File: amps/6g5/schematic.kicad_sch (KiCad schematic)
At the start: 97 parts, among them SW1 AC

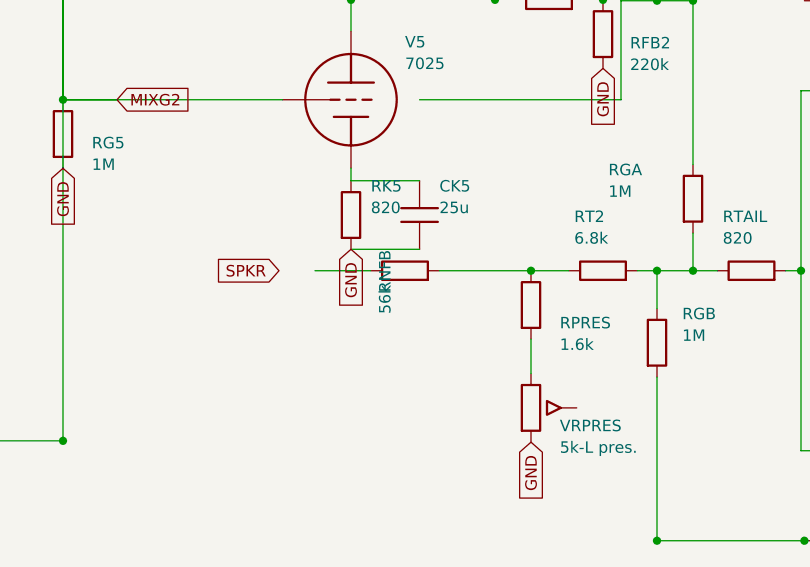
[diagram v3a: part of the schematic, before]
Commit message: Fix: 6G5 RNFB lettered vertically — label_rot pins the FILE angle
The re-shoot caught it at crop zoom: pinning label_rot=0 on a rot-90 body
renders the block vertically, because the renderer treats a property's angle
as symbol-relative — the compensation sym() applies by default (360 - rot)
was being overridden to nothing. The pin was redundant anyway: the authored
under-the-part anchor is the actual fix, and the default compensation
already letters it horizontally. Verified against the live render.

🤖 Generated with [Claude Code](https://claude.com/claude-code)

Co-Authored-By: Claude Fable 5 <noreply@anthropic.com>
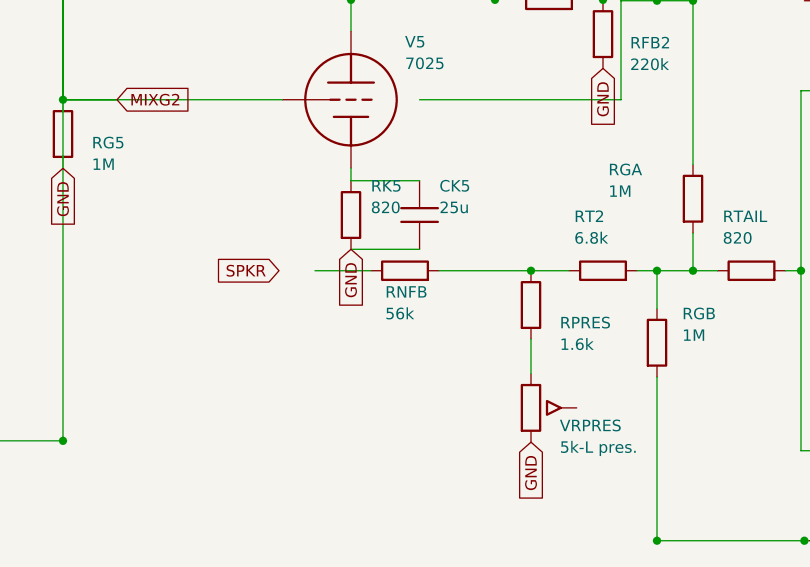
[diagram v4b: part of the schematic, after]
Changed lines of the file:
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@@
   (symbol (lib_id "cx:R") (at 216.745 109.82 90) (unit 1)
     (in_bom yes) (on_board yes)
-    (property "Reference" "RNFB" (at 214.545 112.22 0) (effects (font (size 1.27 1.27)) (justify left)))
-    (property "Value" "56k" (at 214.545 114.62 0) (effects (font (size 1.27 1.27)) (justify left))))
+    (property "Reference" "RNFB" (at 214.545 112.22 270) (effects (font (size 1.27 1.27)) (justify left)))
+    (property "Value" "56k" (at 214.545 114.62 270) (effects (font (size 1.27 1.27)) (justify left))))
   (wire (pts (xy 220.555 109.82) (xy 230.745 109.82))
     (stroke (width 0) (type default)))

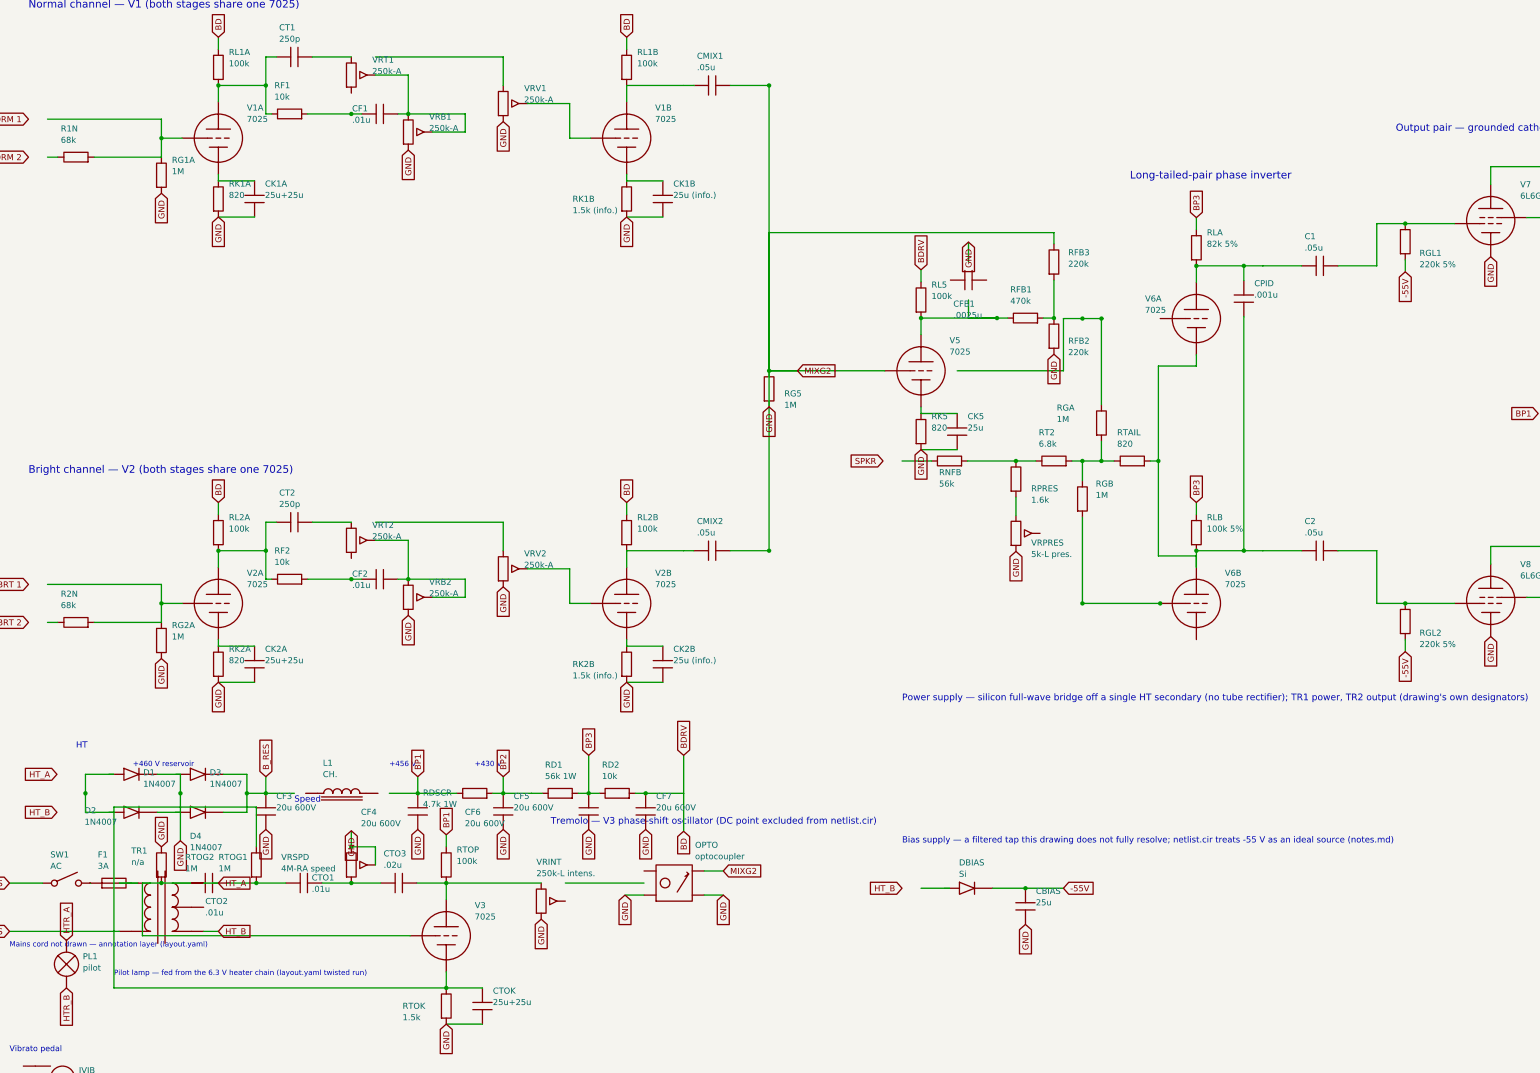
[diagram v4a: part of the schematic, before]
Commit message: Fix: deterministic schematic ids and wires split at every join
- _u() is uuid5 over (amp id, emission order), so a regeneration of an
  unchanged script is byte-identical and a drift gate becomes possible
- write() splits wire segments at symbol pins, wire ends and junction dots,
  so the file connects exactly what the drawing shows under KiCad's
  endpoint-only semantics (270 pins were on a wire's interior; net
  partitions unchanged on all 38 sheets)
- all sheets regenerated; aa864-bassman title block was stale (draft) and
  now matches meta.yaml (verified)

Co-Authored-By: Claude Fable 5.1 <noreply@anthropic.com>
Claude-Session: https://claude.ai/code/session_01KBMfdh37HmCL2iWcBiL5J1
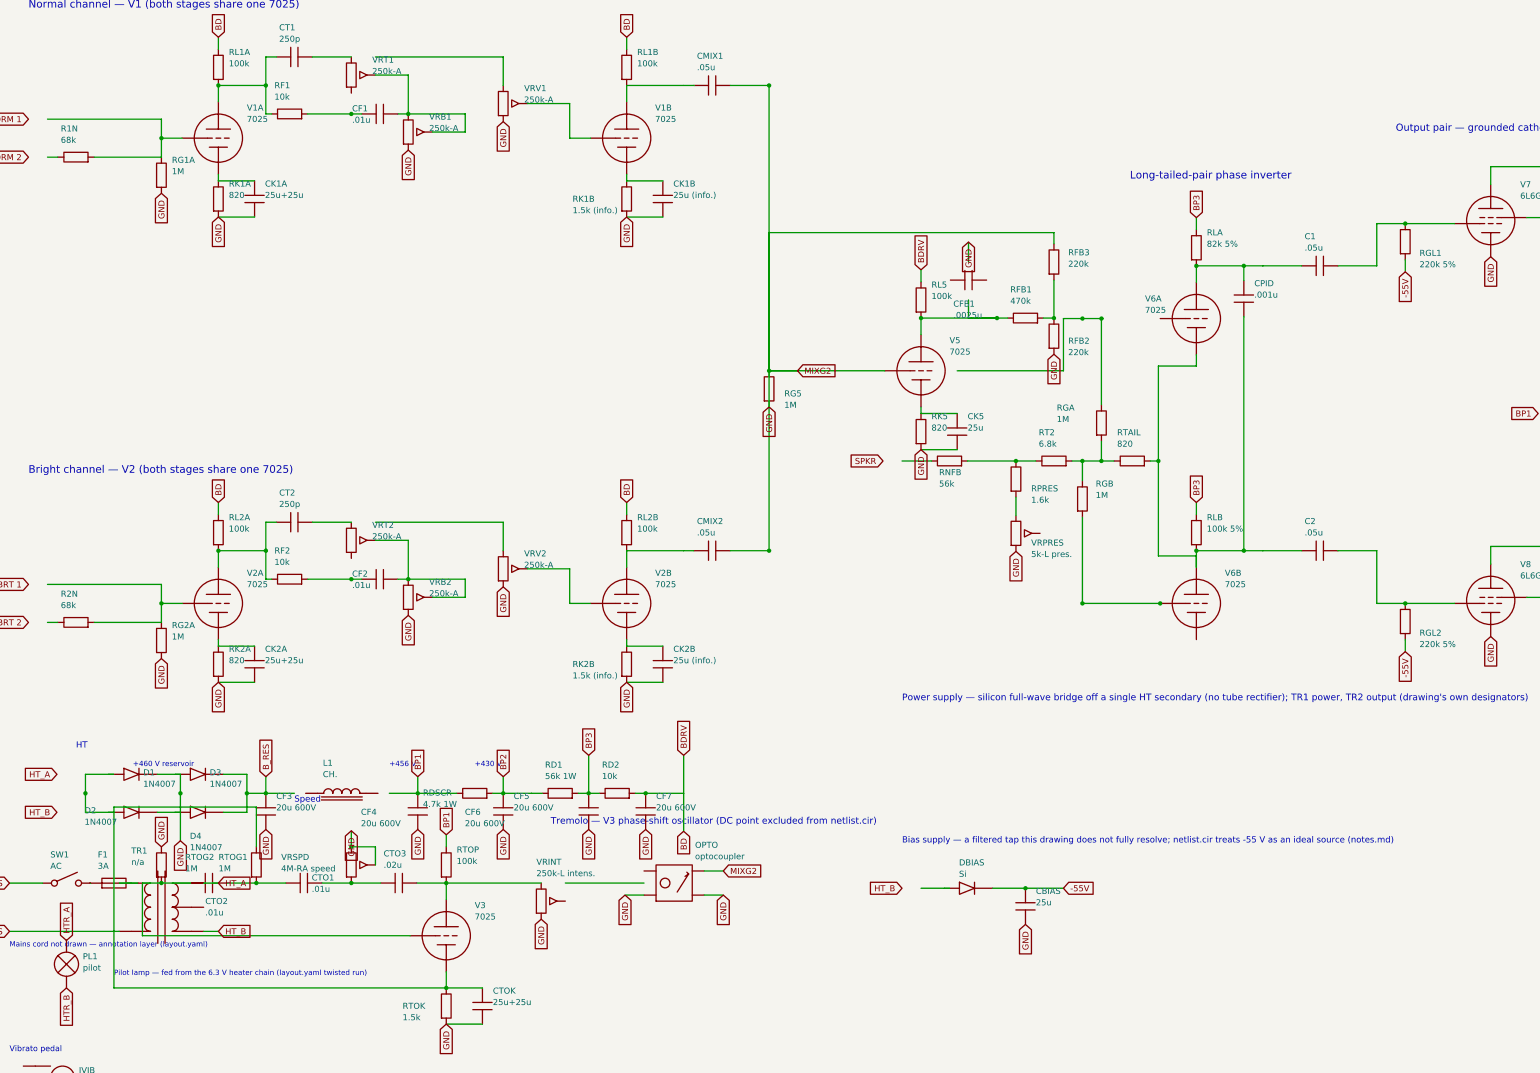
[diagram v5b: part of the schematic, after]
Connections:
- net GND: now also D3.1 (A), D4.1 (A)
- net at CTOK.1, RTOG1.1, RTOK.1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: now also D1.1 (A), D2.1 (A)

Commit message: Fix: schematic wiring on 6g3, 6g4, 6g5, 6g6b
- long-tailed pair tail moved off section B's plate to its cathode (6g3,
  6g4, 6g5); 6g4 V8 plate lead was drawn under its grounded cathode
- 6g6b: all five OT leads on bare coordinates with the secondary drawn on
  the primary side; bias line taken off the bleeder's grounded end (NBIAS
  and GND one net); both tone networks rebuilt; mixing bus ran through
  V3A's bottle
- eight parts shorted end to end, invisible to the pin check: 6g4 RGL1;
  6g5 RG5 (mixing node on ground); 6g6b C11, RG4B, RNFB, RTAIL, RTN1, VR3
- 6g5: treble pot runs off each other's lug, driver run 12 mm short of
  V6A grid, CFB1 rotated but wired upright, choke leads short both ends
- five dated waivers (bridge rectifier centre tap, footswitch terminal
  not lettered on the source, mains side outside the drawing, VR7's
  undesignated cap)
- OPEN, not guessed: 6g5 presence network is drawn as a DC path to ground
  (RPRES + pot in series) while netlist.cir has RT2 to ground and calls the
  network DC-neutral; sources do not settle it — sheet stays unclaimed

Co-Authored-By: Claude Fable 5.1 <noreply@anthropic.com>
Claude-Session: https://claude.ai/code/session_01KBMfdh37HmCL2iWcBiL5J1
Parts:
- removed CF7: 20u 600V, symbol cx:C
- removed JSPK: spkr, symbol cx:JACK
- removed L1: CH., symbol cx:CHOKE
- removed RLA: 82k 5%, symbol cx:R
- removed RNFB: 56k, symbol cx:R
- removed RSC1: 470 1W, symbol cx:R
- removed RT2: 6.8k, symbol cx:R
- removed RTOK: 1.5k, symbol cx:R
- added CTOK: 25u+25u, symbol cx:C
- added D2: 1N4007, symbol cx:DIODE_SS
- added RDSCR: 4.7k 1W, symbol cx:R
- added RGB: 1M, symbol cx:R
- added RLB: 100k 5%, symbol cx:R
- added RPRES: 1.6k, symbol cx:R
- added TR1: n/a, symbol cx:PT
- added TR2: n/a, symbol cx:OT_PP
- CF7: renamed from TR1; value n/a -> 20u 600V; symbol cx:PT -> cx:C
- JSPK: renamed from D2; value 1N4007 -> spkr; symbol cx:DIODE_SS -> cx:JACK
- L1: renamed from RDSCR; value 4.7k 1W -> CH.; symbol cx:R -> cx:CHOKE
- RGL2: renamed from TR2; value n/a -> 220k 5%; symbol cx:OT_PP -> cx:R
- RLA: renamed from RLB; value 100k 5% -> 82k 5%
- RNFB: renamed from RGB; value 1M -> 56k
- RSC1: renamed from RGL2; value 220k 5% -> 470 1W
- RT2: renamed from RPRES; value 1.6k -> 6.8k
- RTOK: renamed from CTOK; value 25u+25u -> 1.5k; symbol cx:C -> cx:R
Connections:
- net -55V: now also RGL2.2; no longer RSC1.2
- net BD: now also CF7.1; no longer RL5.1
- net BP1: now also L1.2, RDSCR.1, TR2.2 (CT); no longer L1.1
- net BP2: now also RSC1.2, RDSCR.2; no longer L1.2
- net BP3: now also RLB.1
- net BRT 1: now also R2N.2, RG2A.1, V2A.2 (G)
- net BRT 2: now also R2N.1
- net B_RES: now also L1.1
- net GND: now also CF7.2, CFB1.1, JVIB.2 (S), CTOK.2, D2.2 (K); no longer CMIX1.2, CMIX2.2, JSPK.2 (K), OPTO.3 (P1), RFB3.1, RG5.1, V5.2 (G)
- net HT_A: now also TR1.3 (HT_A); no longer CF7.3 (HT_A)
- net HT_B: now also DBIAS.1 (A), TR1.5 (HT_B); no longer CF7.5 (HT_B)
- net MAINS: now also TR1.2 (PRI_2); no longer CF7.2 (PRI_2)
- net NORM 1: now also R1N.2, RG1A.1, V1A.2 (G)
- net NORM 2: now also R1N.1
- net SPKR: now also JSPK.1 (T), RNFB.1, TR2.4 (SEC_H); no longer RGL2.4 (SEC_H)
- net at D1.1 (A), RTOG1.1, RTOK.1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: now also CTOK.1, D2.1 (A); no longer JSPK.1 (A)
- net at VRINT.2 (W): now also OPTO.1 (L1)
- net at C1.1, CPID.1, V6A.1 (P): now also RLA.2
- net at C2.1, CPID.2, V6B.1 (P): now also RLB.2; no longer RLA.2, RTAIL.2, V6A.3 (K)
- net at RT2.1: now also RNFB.2, RPRES.1
- net at RGA.2, RTAIL.1: now also RT2.2, RGB.1; no longer RNFB.1
- net at C2.2, V8.2 (G1): now also RGL2.1; no longer RSC1.1
- net at V8.1 (P): now also TR2.3 (PRI_B); no longer RGL2.3 (PRI_B)
- net at VRV1.1: now also VRT1.2 (W)
- net at F1.2: now also TR1.1 (PRI_1); no longer CF7.1 (PRI_1)
- net at VRV2.1: now also VRT2.2 (W)
- net at RFB1.1, RL5.2, V5.1 (P): now also CFB1.2
- net at VRB2.1, VRB2.2 (W): now also VRT2.3; no longer VRT2.2 (W)
- net at V7.1 (P): now also TR2.1 (PRI_A); no longer RGL2.1 (PRI_A)
- net at V7.3 (G2): now also RSC1.1
- net at RGA.1: now also V6A.2 (G)
- net at V6B.2 (G): now also RGB.2; no longer RNFB.2
- net at V6B.3 (K): now also RTAIL.2, V6A.3 (K)
- net at VRPRES.1: now also VRPRES.2 (W), RPRES.2; no longer RT2.2
- net at VRB1.1, VRB1.2 (W): now also VRT1.3; no longer VRT1.2 (W)
- new net: JSPK.2 (S), TR2.5 (SEC_C)
- new net BDRV: RL5.1
- new net MIXG2: CMIX1.2, CMIX2.2, OPTO.3 (P1), RFB3.1, RG5.1, V5.2 (G)
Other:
- note added: "56k/10k dropper — illustrative; BP3/BDRV/BD are driven anchors (see header). The driver rail sits above the reservoir this chain hangs from, so no tap off it is drawn."
- note removed: "56k/10k dropper — illustrative; BP3/BDRV/BD are driven anchors (see header)"
- moved on the sheet: CFB1, RG5, RLA, RNFB, RSC1, RT2

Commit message: Fix: 6g5 presence network redrawn from the factory sheet; four faults
Read against the published Fender Pro-Amp 6G5 sheet (A-FJ) and its layout:

- RPRES was drawn in series with the Presence pot, so the phase-inverter
  tail's only DC path to ground ran through both and the pot varied the
  tail resistance. The sheet draws it as a FOOT resistor straight to
  ground, with the pot paralleling it.
- the presence capacitor was missing from the corpus entirely. It is what
  makes that branch AC-only -- the property netlist.cir already asserted.
  Added as CPRES, 0.1 uF; the 200 V is read off the layout sheet's own
  '.1-200' lettering, not defaulted from the notice's 400 V.
- RPRES is 1500, not the 1.6k we published, and it is a foot resistor,
  not the 'series resistor' the parts list called it.
- RNFB is 22k, not 56k. Traced end to end from the OT secondary hot.

netlist.cir, meta.yaml and notes.md all said the NFB/presence network was
AC-only and DC-neutral. Only the pot branch is: the foot resistor and the
feedback return are real DC paths. Corrected, and the netlist's RT2 -> 0
is now declared in sch_map.yaml as the DC simplification it is, with the
reason written out. No gated node depends on it (KPI and JPI carry no
chart value).

6g5 now passes verify_schematic_nets -- the last sheet that did not --
but stays draft and unclaimed pending review.

Co-Authored-By: Claude Opus 5 (1M context) <noreply@anthropic.com>
Claude-Session: https://claude.ai/code/session_01KBMfdh37HmCL2iWcBiL5J1
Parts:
- removed CF5, CF7: 20u 600V, symbol cx:C
- removed D2: 1N4007, symbol cx:DIODE_SS
- removed RPRES: 1.6k, symbol cx:R
- removed RSC1: 470 1W, symbol cx:R
- added CF6: 20u 600V, symbol cx:C
- added CPRES: .1u 200V, symbol cx:C
- added D3: 1N4007, symbol cx:DIODE_SS
- added RGB: 1M, symbol cx:R
- added SW1: AC, symbol cx:SWITCH
- added TR2: n/a, symbol cx:OT_PP
- CF7: renamed from SW1; value AC -> 20u 600V; symbol cx:SWITCH -> cx:C
- RGL2: renamed from TR2; value n/a -> 220k 5%; symbol cx:OT_PP -> cx:R
- RNFB: renamed from RGB; value 1M -> 22k
- RPRES: renamed from VRPRES; value 5k-L pres. -> 1.5k; symbol cx:POT -> cx:R
- RSC1: renamed from RGL2; value 220k 5% -> 470 1W
- VRPRES: renamed from RNFB; value 56k -> 5k-L pres.; symbol cx:R -> cx:POT
- renumbered CF6 to CF5, D3 to D2
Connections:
- net -55V: now also RGL2.2; no longer RSC1.2
- net BD: now also CF7.1
- net BP1: now also TR2.2 (CT); no longer RGL2.2 (CT)
- net BP2: now also CF5.1, RSC1.2
- net BP3: now also CF6.1; no longer CF5.1
- net B_RES: now also D3.2 (K); no longer D2.2 (K)
- net GND: now also CF7.2, D2.2 (K), RPRES.2, CF6.2, CPRES.2, D3.1 (A); no longer D2.1 (A), RPRES.3
- net MAINS: now also SW1.1; no longer CF7.1
- net SPKR: now also RNFB.1, TR2.4 (SEC_H); no longer RGL2.4 (SEC_H), VRPRES.1
- net at F1.1: now also SW1.2; no longer CF7.2
- net at CTOK.1, D1.1 (A), RTOG1.1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: now also D2.1 (A)
- net at RGL2.1: now also C2.2, V8.2 (G1); no longer V7.1 (P)
- net at V8.1 (P): now also TR2.3 (PRI_B); no longer RGL2.3 (PRI_B)
- net at JSPK.2 (S): now also TR2.5 (SEC_C); no longer RGL2.5 (SEC_C)
- net at V7.3 (G2): now also RSC1.1
- net at RT2.1, VRPRES.2 (W): now also RNFB.2, RPRES.1, VRPRES.1
- net at RGA.2, RT2.2, RTAIL.1: now also RGB.1; no longer RNFB.1
- net at V6B.2 (G): now also RGB.2; no longer RNFB.2
- new net: CPRES.1, VRPRES.3
- new net: TR2.1 (PRI_A), V7.1 (P)
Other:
- note added: "1"
- note added: "2"
- note added: "3"
- note added: "4"
- note added: "5"
- note added: "6"
- note added: "7"
- note added: "8"
- moved on the sheet: CF5, D2, RNFB, RSC1
